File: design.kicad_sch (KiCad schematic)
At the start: 80 parts, among them J1 2601-3108, J10 Conn_01x04, J11 Conn_01x04, J12 Conn_01x03, J13 Conn_01x03, J14 BM04B-SRSS-TB_LF__SN_, J2 2601-3108, J3 2601-3108, J4 TYPE-C-31-M-12, J5 SKEDD-UPDI-4, J6 Conn_01x04, J7 Conn_01x04, J8 Conn_01x04, J9 Conn_01x04, U1 ATtiny1616-S, U2 AP2112K-3.3, U3 CP2105

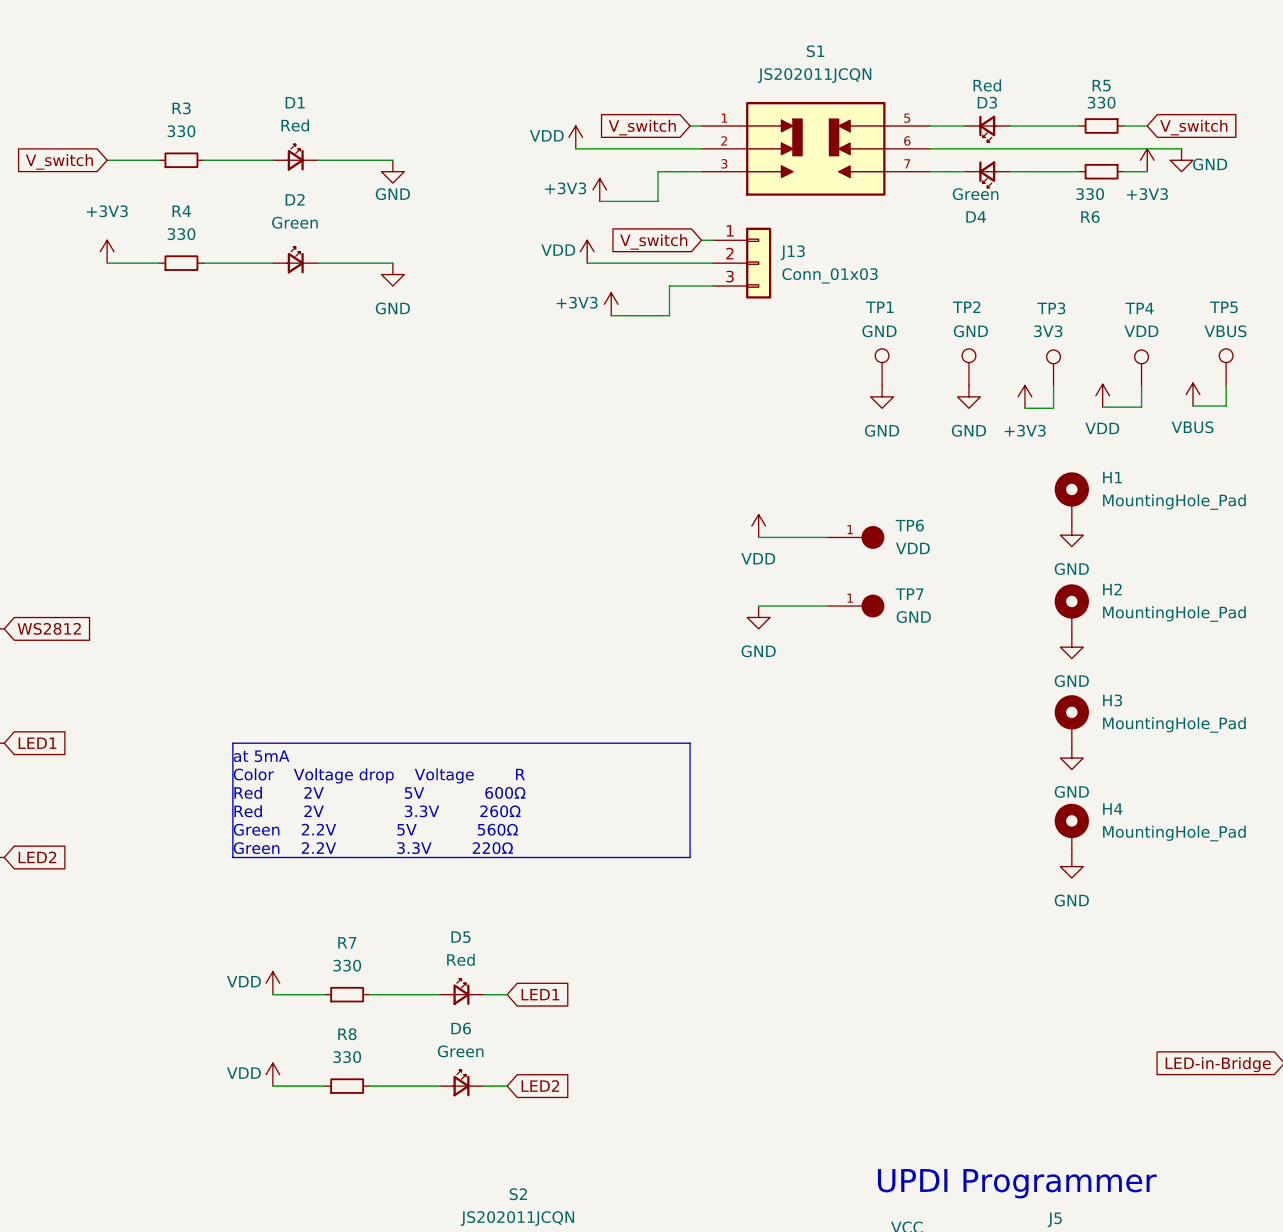
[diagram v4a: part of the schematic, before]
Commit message: update LED resistor values
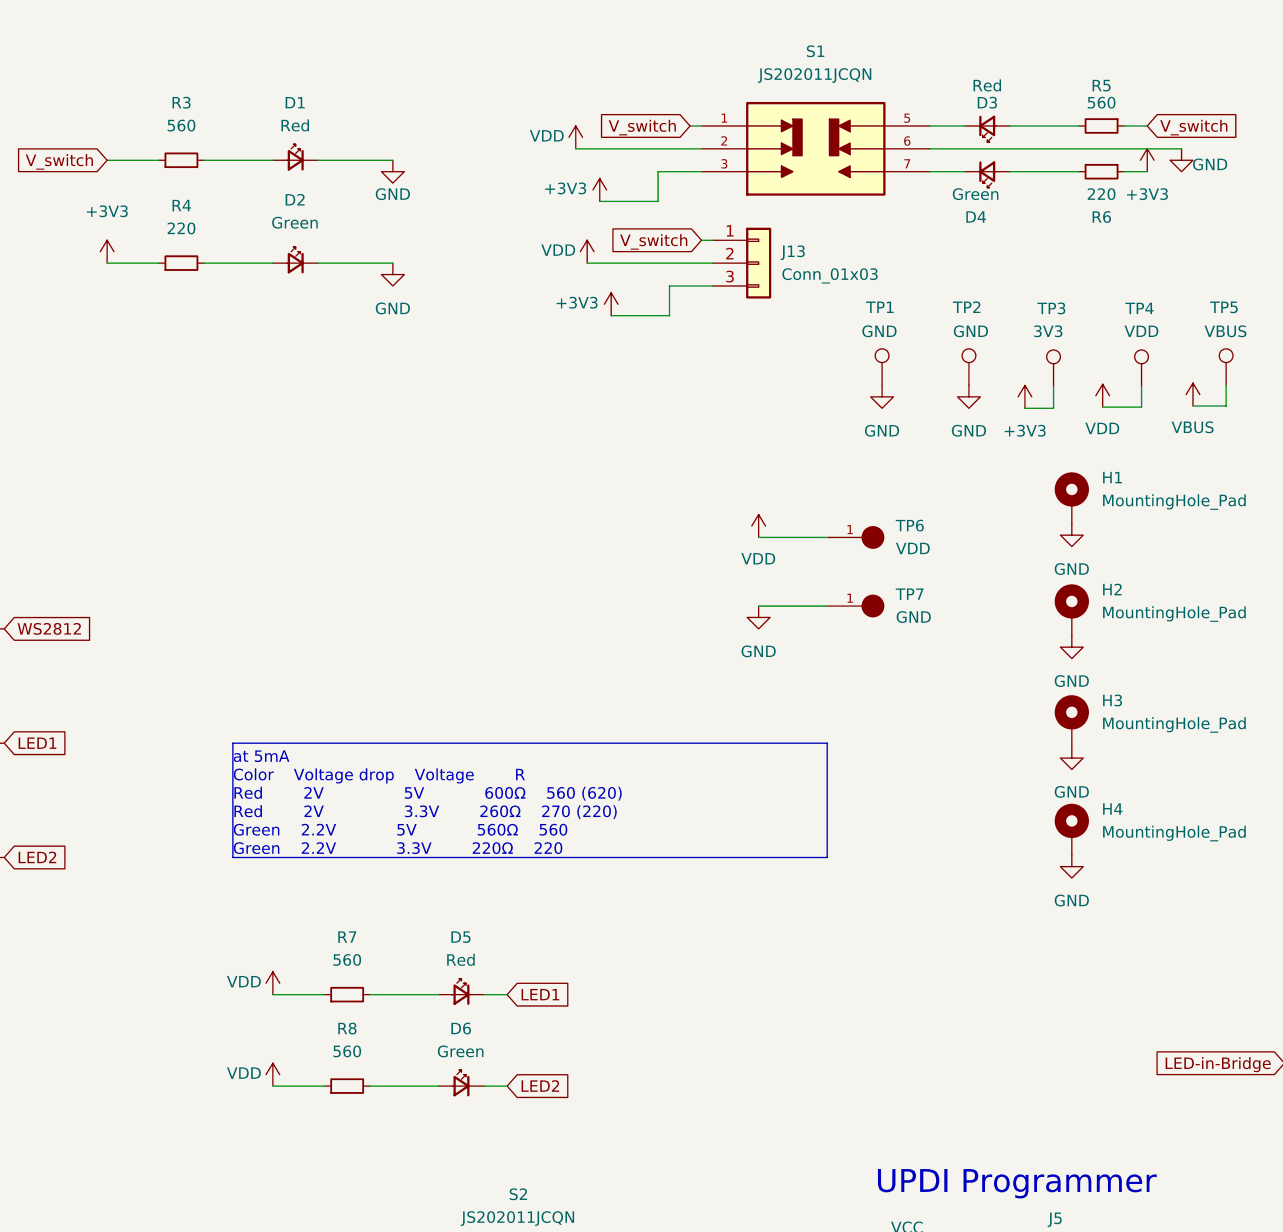
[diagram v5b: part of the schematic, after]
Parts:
- R3, R5, R7, R8: value 330 -> 560
- R4, R6: value 330 -> 220
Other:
- note added: "at 5mA Color Voltage drop Voltage R Red 2V 5V 600Ω 560 (620) Red 2V 3.3V 260Ω 270 (220) Green 2.2V 5V 560Ω 560 Green 2.2V 3.3V 220Ω 220"
- note removed: "at 5mA Color Voltage drop Voltage R Red 2V 5V 600Ω Red 2V 3.3V 260Ω Green 2.2V 5V 560Ω Green 2.2V 3.3V 220Ω"
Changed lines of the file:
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@@
     (stroke (width 0) (type default) (color 0 0 0 0))
   )
-  (polyline (pts (xy 213.36 93.98) (xy 213.36 106.68))
+  (polyline (pts (xy 228.6 93.98) (xy 228.6 106.68))
     (stroke (width 0) (type default) (color 0 0 0 0))
   )
@@
     (stroke (width 0) (type default) (color 0 0 0 0))
   )
-  (polyline (pts (xy 213.36 106.68) (xy 162.56 106.68))
+  (polyline (pts (xy 228.6 106.68) (xy 162.56 106.68))
     (stroke (width 0) (type default) (color 0 0 0 0))
   )
@@
     (stroke (width 0) (type default) (color 0 0 0 0))
   )
-  (polyline (pts (xy 162.56 93.98) (xy 213.36 93.98))
+  (polyline (pts (xy 162.56 93.98) (xy 228.6 93.98))
     (stroke (width 0) (type default) (color 0 0 0 0))
   )
@@
     (effects (font (size 1.27 1.27)) (justify left bottom))
   )
-  (text "at 5mA\nColor	Voltage drop	Voltage    	R\nRed		2V				5V			600Ω\nRed		2V				3.3V		260Ω\nGreen	2.2V			5V			560Ω\nGreen	2.2V			3.3V		220Ω"
+  (text "at 5mA\nColor	Voltage drop	Voltage    	R\nRed		2V				5V			600Ω	560 (620)\nRed		2V				3.3V		260Ω	270 (220)\nGreen	2.2V			5V			560Ω	560\nGreen	2.2V			3.3V		220Ω	220"
     (at 162.56 106.68 0)
     (effects (font (size 1.27 1.27)) (justify left bottom))
@@
   (symbol (lib_id "Device:R_Small") (at 156.845 40.64 90) (unit 1)
     (in_bom yes) (on_board yes) (fields_autoplaced)
-    (property "Reference" "R4" (id 0) (at 156.845 34.925 90))
-    (property "Value" "330" (id 1) (at 156.845 37.465 90))
+    (property "Reference" "R4" (id 0) (at 156.845 34.29 90))
+    (property "Value" "220" (id 1) (at 156.845 36.83 90))
     (property "Footprint" "Resistor_SMD:R_0805_2012Metric" (id 2) (at 156.845 40.64 0)
       (effects (font (size 1.27 1.27)) hide)
@@
   (symbol (lib_id "power:GND") (at 71.12 256.54 0) (unit 1)
     (in_bom yes) (on_board yes) (fields_autoplaced)
-    (property "Reference" "#PWR?" (id 0) (at 71.12 262.89 0)
+    (property "Reference" "#PWR0189" (id 0) (at 71.12 262.89 0)
       (effects (font (size 1.27 1.27)) hide)
     )
@@
   (symbol (lib_id "Device:R_Small") (at 175.26 121.92 90) (unit 1)
     (in_bom yes) (on_board yes) (fields_autoplaced)
-    (property "Reference" "R7" (id 0) (at 175.26 116.205 90))
-    (property "Value" "330" (id 1) (at 175.26 118.745 90))
+    (property "Reference" "R7" (id 0) (at 175.26 115.57 90))
+    (property "Value" "560" (id 1) (at 175.26 118.11 90))
     (property "Footprint" "Resistor_SMD:R_0805_2012Metric" (id 2) (at 175.26 121.92 0)
       (effects (font (size 1.27 1.27)) hide)
@@
   (symbol (lib_id "Device:R_Small") (at 156.845 29.21 90) (unit 1)
     (in_bom yes) (on_board yes) (fields_autoplaced)
-    (property "Reference" "R3" (id 0) (at 156.845 23.495 90))
-    (property "Value" "330" (id 1) (at 156.845 26.035 90))
+    (property "Reference" "R3" (id 0) (at 156.845 22.86 90))
+    (property "Value" "560" (id 1) (at 156.845 25.4 90))
     (property "Footprint" "Resistor_SMD:R_0805_2012Metric" (id 2) (at 156.845 29.21 0)
       (effects (font (size 1.27 1.27)) hide)
@@
   (symbol (lib_id "Device:R_Small") (at 259.08 30.48 270) (unit 1)
     (in_bom yes) (on_board yes)
-    (property "Reference" "R6" (id 0) (at 257.81 35.56 90))
-    (property "Value" "330" (id 1) (at 257.81 33.02 90))
+    (property "Reference" "R6" (id 0) (at 259.08 35.56 90))
+    (property "Value" "220" (id 1) (at 259.08 33.02 90))
     (property "Footprint" "Resistor_SMD:R_0805_2012Metric" (id 2) (at 259.08 30.48 0)
       (effects (font (size 1.27 1.27)) hide)
@@
   (symbol (lib_id "Device:R_Small") (at 175.26 132.08 90) (unit 1)
     (in_bom yes) (on_board yes) (fields_autoplaced)
-    (property "Reference" "R8" (id 0) (at 175.26 126.365 90))
-    (property "Value" "330" (id 1) (at 175.26 128.905 90))
+    (property "Reference" "R8" (id 0) (at 175.26 125.73 90))
+    (property "Value" "560" (id 1) (at 175.26 128.27 90))
     (property "Footprint" "Resistor_SMD:R_0805_2012Metric" (id 2) (at 175.26 132.08 0)
       (effects (font (size 1.27 1.27)) hide)
@@
     (in_bom yes) (on_board yes)
     (property "Reference" "R5" (id 0) (at 259.08 20.955 90))
-    (property "Value" "330" (id 1) (at 259.08 22.86 90))
+    (property "Value" "560" (id 1) (at 259.08 22.86 90))
     (property "Footprint" "Resistor_SMD:R_0805_2012Metric" (id 2) (at 259.08 25.4 0)
       (effects (font (size 1.27 1.27)) hide)
@@
     )
     (path "/3b010638-00df-47c0-8bf4-5465e4ce7746"
-      (reference "#PWR?") (unit 1) (value "GND") (footprint "")
+      (reference "#PWR0189") (unit 1) (value "GND") (footprint "")
     )
     (path "/5005112b-a25c-4019-a0f7-bec67dd371e4"
@@
     )
     (path "/484da902-60c6-4980-9a91-4f667955b0e8"
-      (reference "R3") (unit 1) (value "330") (footprint "Resistor_SMD:R_0805_2012Metric")
+      (reference "R3") (unit 1) (value "560") (footprint "Resistor_SMD:R_0805_2012Metric")
     )
     (path "/0e89c407-3205-4c62-a491-3291420c5ad0"
-      (reference "R4") (unit 1) (value "330") (footprint "Resistor_SMD:R_0805_2012Metric")
+      (reference "R4") (unit 1) (value "220") (footprint "Resistor_SMD:R_0805_2012Metric")
     )
     (path "/bcf61e20-6cf8-46b9-9f95-d5e631d20676"
-      (reference "R5") (unit 1) (value "330") (footprint "Resistor_SMD:R_0805_2012Metric")
+      (reference "R5") (unit 1) (value "560") (footprint "Resistor_SMD:R_0805_2012Metric")
     )
     (path "/72f13b47-0aa0-4ea7-a1ab-fd196a1c1813"
-      (reference "R6") (unit 1) (value "330") (footprint "Resistor_SMD:R_0805_2012Metric")
+      (reference "R6") (unit 1) (value "220") (footprint "Resistor_SMD:R_0805_2012Metric")
     )
     (path "/42965c34-d4b3-417b-ac70-1b8024990edc"
-      (reference "R7") (unit 1) (value "330") (footprint "Resistor_SMD:R_0805_2012Metric")
+      (reference "R7") (unit 1) (value "560") (footprint "Resistor_SMD:R_0805_2012Metric")
     )
     (path "/aa06b4af-70da-4895-9f86-987878ddf602"
-      (reference "R8") (unit 1) (value "330") (footprint "Resistor_SMD:R_0805_2012Metric")
+      (reference "R8") (unit 1) (value "560") (footprint "Resistor_SMD:R_0805_2012Metric")
     )
     (path "/5d57726e-0434-4089-b57f-b38108417a5f"

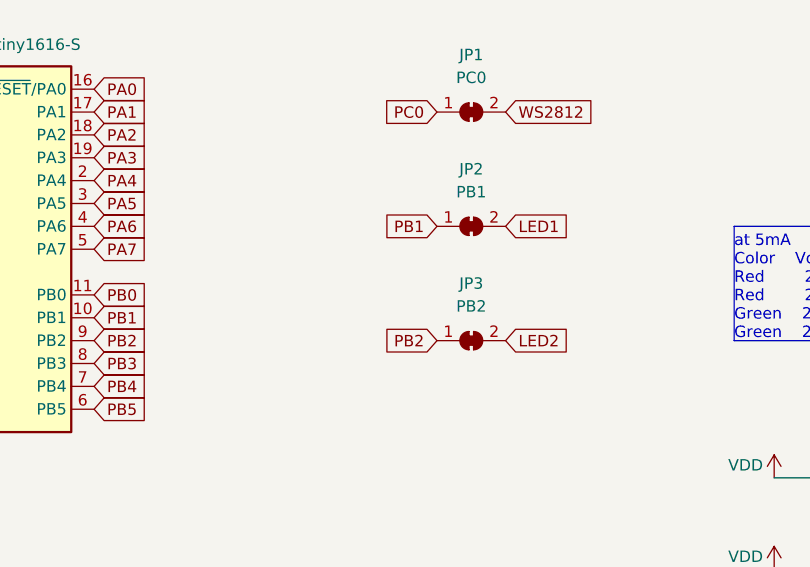
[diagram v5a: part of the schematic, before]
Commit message: change LEDs to pin PB2/PB3 not to use the i2c pins
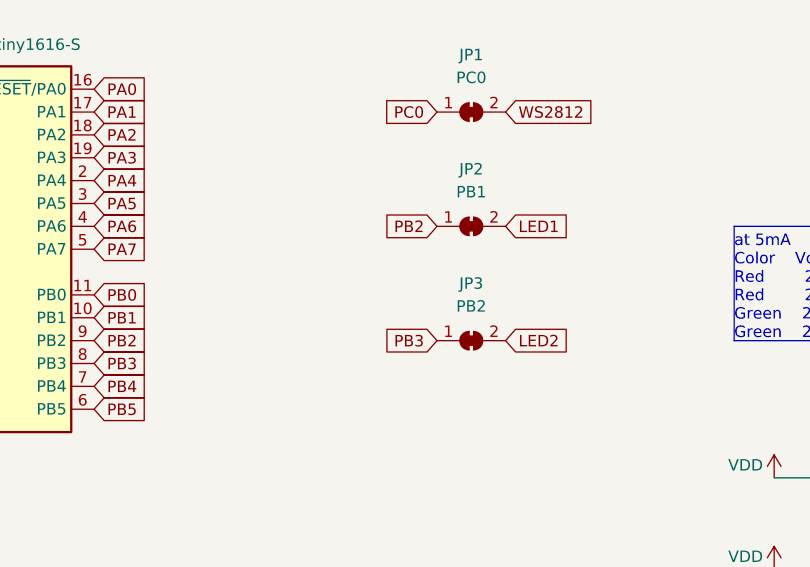
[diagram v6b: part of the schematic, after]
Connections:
- net PB1: no longer JP2.1 (A)
- net PB2: now also JP2.1 (A); no longer JP3.1 (A)
- net PB3: now also JP3.1 (A)

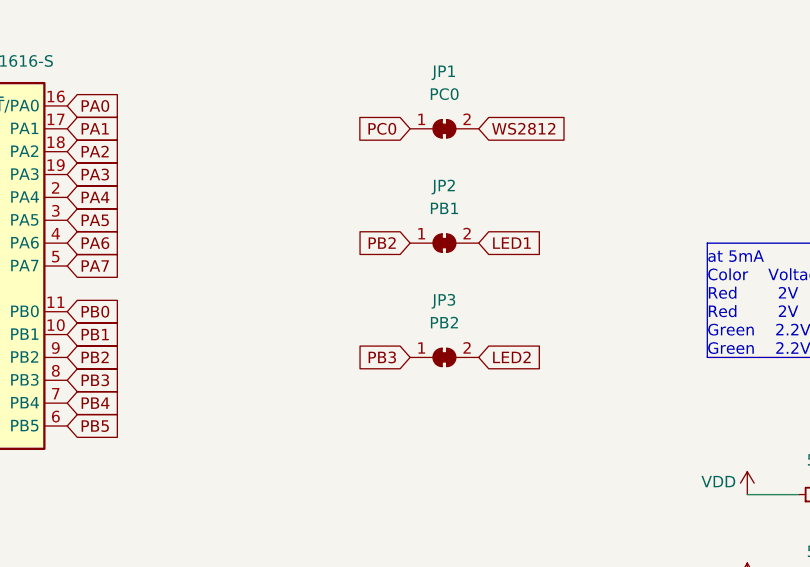
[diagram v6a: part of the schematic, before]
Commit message: Route LEDs to own pins
closes #2
Use PA4 and PA5 for the LEDs. This pins have PWM and are not used.
correct the silk screen.
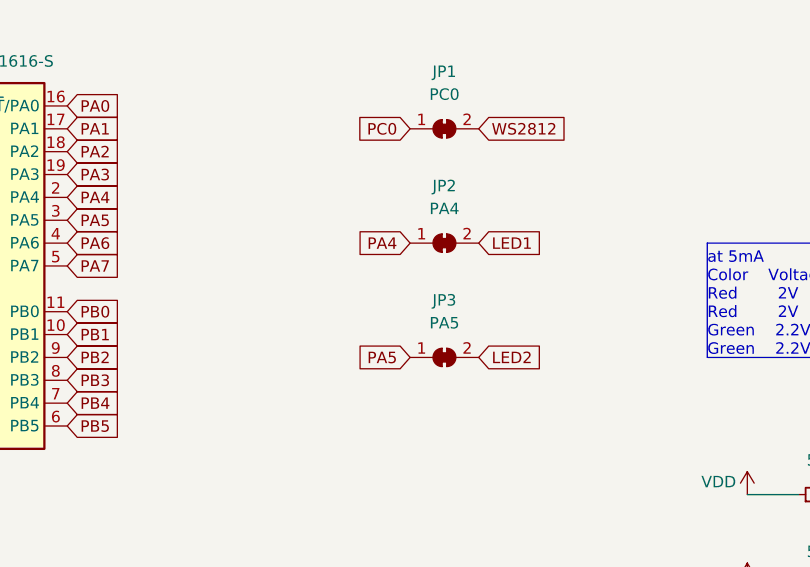
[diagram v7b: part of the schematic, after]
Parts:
- JP2: value PB1 -> PA4
- JP3: value PB2 -> PA5
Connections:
- net PA4: now also JP2.1 (A)
- net PA5: now also JP3.1 (A)
- net PB2: no longer JP2.1 (A)
- net PB3: no longer JP3.1 (A)
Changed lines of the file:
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@@
     )
   )
-  (global_label "PB2" (shape input) (at 129.54 93.98 180) (fields_autoplaced)
+  (global_label "PA4" (shape input) (at 129.54 93.98 180) (fields_autoplaced)
     (effects (font (size 1.27 1.27)) (justify right))
-    (property "Referenzen zwischen Schaltplänen" "${INTERSHEET_REFS}" (id 0) (at 123.4663 94.0594 0)
+    (property "Referenzen zwischen Schaltplänen" "${INTERSHEET_REFS}" (id 0) (at 123.6477 93.9006 0)
       (effects (font (size 1.27 1.27)) (justify right) hide)
     )
@@
     )
   )
-  (global_label "PB3" (shape input) (at 129.54 106.68 180) (fields_autoplaced)
+  (global_label "PA5" (shape input) (at 129.54 106.68 180) (fields_autoplaced)
     (effects (font (size 1.27 1.27)) (justify right))
-    (property "Referenzen zwischen Schaltplänen" "${INTERSHEET_REFS}" (id 0) (at 123.4663 106.6006 0)
+    (property "Referenzen zwischen Schaltplänen" "${INTERSHEET_REFS}" (id 0) (at 123.6477 106.6006 0)
       (effects (font (size 1.27 1.27)) (justify right) hide)
     )
@@
     (in_bom yes) (on_board yes)
     (property "Reference" "JP3" (id 0) (at 133.35 100.33 0))
-    (property "Value" "PB2" (id 1) (at 133.35 102.87 0))
+    (property "Value" "PA5" (id 1) (at 133.35 102.87 0))
     (property "Footprint" "Jumper:SolderJumper-2_P1.3mm_Bridged_Pad1.0x1.5mm" (id 2) (at 133.35 106.68 0)
       (effects (font (size 1.27 1.27)) hide)
@@
     (in_bom yes) (on_board yes)
     (property "Reference" "JP2" (id 0) (at 133.35 87.63 0))
-    (property "Value" "PB1" (id 1) (at 133.35 90.17 0))
+    (property "Value" "PA4" (id 1) (at 133.35 90.17 0))
     (property "Footprint" "Jumper:SolderJumper-2_P1.3mm_Bridged_Pad1.0x1.5mm" (id 2) (at 133.35 93.98 0)
       (effects (font (size 1.27 1.27)) hide)
@@
     )
     (path "/350eccb5-7cc4-4388-92bb-b4f919a6433f"
-      (reference "JP2") (unit 1) (value "PB1") (footprint "Jumper:SolderJumper-2_P1.3mm_Bridged_Pad1.0x1.5mm")
+      (reference "JP2") (unit 1) (value "PA4") (footprint "Jumper:SolderJumper-2_P1.3mm_Bridged_Pad1.0x1.5mm")
     )
     (path "/23e710d7-702a-40ba-9088-48d36a43b3b2"
-      (reference "JP3") (unit 1) (value "PB2") (footprint "Jumper:SolderJumper-2_P1.3mm_Bridged_Pad1.0x1.5mm")
+      (reference "JP3") (unit 1) (value "PA5") (footprint "Jumper:SolderJumper-2_P1.3mm_Bridged_Pad1.0x1.5mm")
     )
     (path "/eaa8d364-f7ce-4c97-8b29-de4ff6423ebd"
